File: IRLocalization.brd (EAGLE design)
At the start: 80 x 80 mm, 24 parts

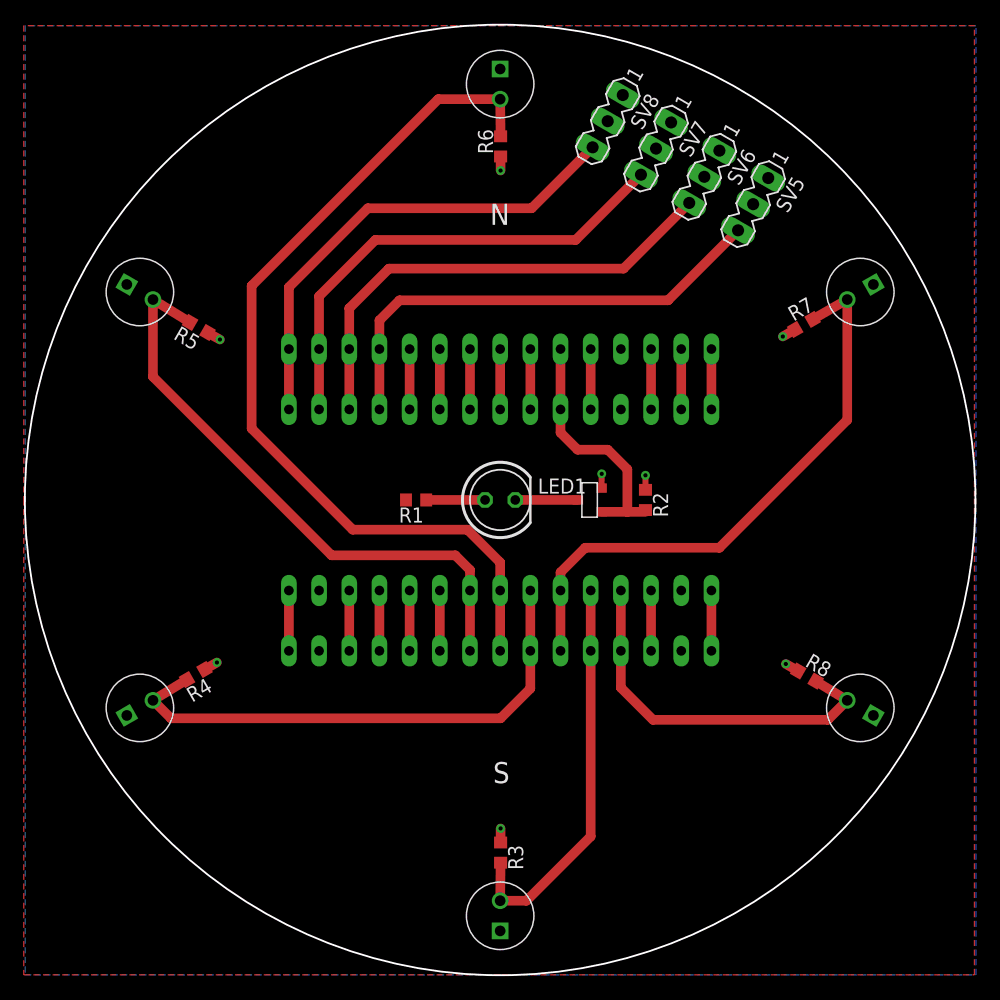
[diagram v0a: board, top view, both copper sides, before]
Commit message: Added mounting holes
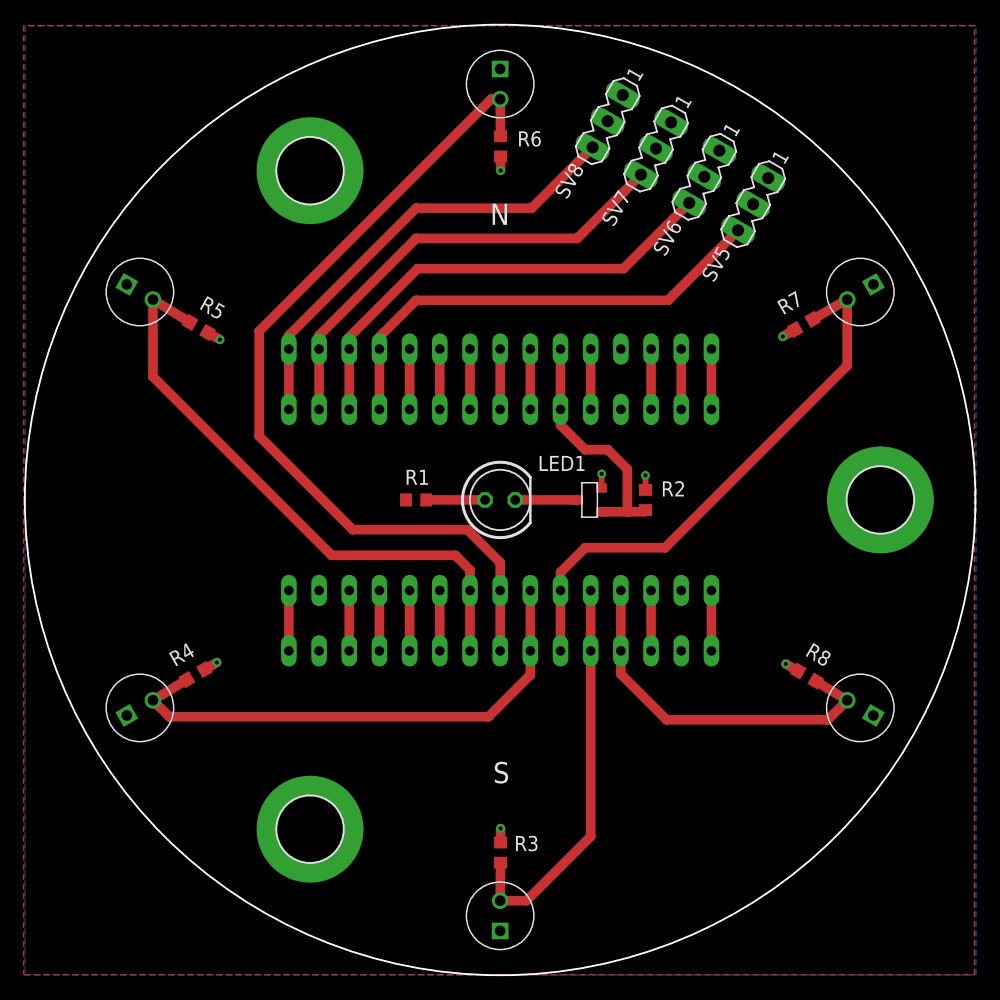
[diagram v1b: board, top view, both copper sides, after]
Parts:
- added H1, H2, H3: MOUNT-PAD-ROUND5.5, holes:5,5-PAD
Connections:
- net N$2 renamed LED+
- net N$4 renamed LED-
- net GND: now also H1.B5,5, H2.B5,5, H3.B5,5
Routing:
- net A4: track 75.6 -> 72.5 mm
- net A2: track 49.5 -> 46.9 mm
- net D12: track 40.7 -> 38.3 mm
- net D11: track 40.9 -> 38.9 mm
- net D10: track 40.8 -> 39.4 mm
- net D9: track 40.8 -> 40.0 mm
- net A3: track 45.0 -> 44.3 mm
- net A0: track 32.1 -> 31.5 mm

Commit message: Fixed orientation for nano headers
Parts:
- moved SV8 50.3 mm to (26.0, 44.0), turned to 0 degrees
- moved SV5 49.1 mm to (26.0, 56.0), turned to 0 degrees
- moved SV7 48.7 mm to (26.0, 48.0), turned to 0 degrees
- moved SV6 48.3 mm to (26.0, 52.0), turned to 0 degrees
- moved SV1 25.4 mm to (50.0, 37.3)
- moved SV2 25.4 mm to (50.0, 62.7), turned to 180 degrees
- moved SV3 15.2 mm to (50.0, 57.6), turned to 180 degrees
- moved SV4 15.2 mm to (50.0, 42.4)
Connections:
- net A0: now also R4.2, U$3.E; no longer R8.2, U$7.E
- net A1: now also R5.2, U$4.E; no longer R3.2, U$2.E
- net A2: now also R3.2, U$2.E; no longer R7.2, U$6.E
- net A3: now also R8.2, U$7.E; no longer R4.2, U$3.E
- net A5: now also R7.2, U$6.E; no longer R5.2, U$4.E
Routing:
- net A4: track 72.5 -> 27.8 mm
- net A2: track 46.9 -> 76.8 mm
- net D12: track 38.3 -> 9.43 mm
- net A0: track 31.5 -> 57.3 mm
- net D11: track 38.9 -> 14.2 mm
- net D10: track 39.4 -> 18.8 mm
- net D9: track 40.0 -> 23.4 mm
- net A5: track 50.4 -> 36.3 mm
- net A3: track 44.3 -> 53.0 mm
- net D3: track 21.0 -> 17.0 mm
- net A1: track 33.8 -> 31.5 mm
